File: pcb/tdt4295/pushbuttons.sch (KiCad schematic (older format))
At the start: 4 parts

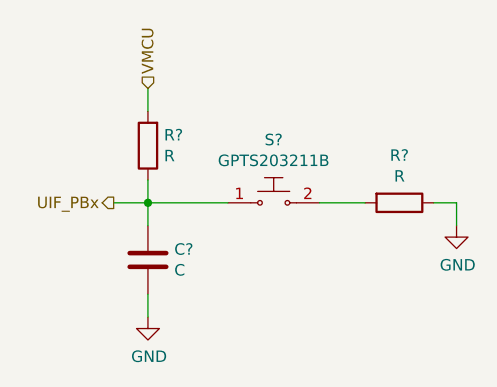
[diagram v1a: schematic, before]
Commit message: add indicator LEDs to power supply
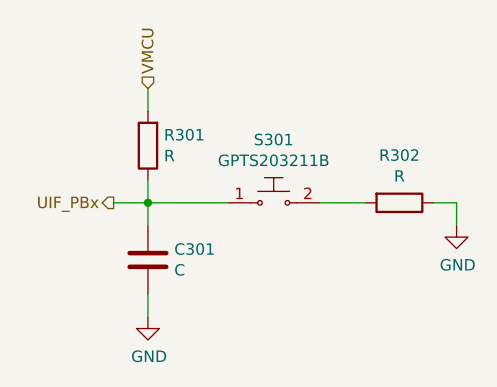
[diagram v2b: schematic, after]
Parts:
- gave numbers to parts that had none: 4
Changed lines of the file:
@@
 $EndDescr
 $Comp
-L Device:R R?
+L Device:R R302
 U 1 1 6137CF49
 P 6650 3150
-F 0 "R?" V 6443 3150 50  0000 C CNN
+F 0 "R302" V 6443 3150 50  0000 C CNN
 F 1 "R" V 6534 3150 50  0000 C CNN
 F 2 "" V 6580 3150 50  0001 C CNN
@@
 $EndComp
 $Comp
-L power:GND #PWR?
+L power:GND #PWR0302
 U 1 1 6137E2C6
 P 6900 3250
-F 0 "#PWR?" H 6900 3000 50  0001 C CNN
+F 0 "#PWR0302" H 6900 3000 50  0001 C CNN
 F 1 "GND" H 6905 3077 50  0000 C CNN
 F 2 "" H 6900 3250 50  0001 C CNN
@@
 $EndComp
 $Comp
-L dk_Pushbutton-Switches:GPTS203211B S?
+L dk_Pushbutton-Switches:GPTS203211B S301
 U 1 1 61381706
 P 6100 3150
-F 0 "S?" H 6100 3425 50  0000 C CNN
+F 0 "S301" H 6100 3425 50  0000 C CNN
 F 1 "GPTS203211B" H 6100 3334 50  0000 C CNN
 F 2 "digikey-footprints:PushButton_12x12mm_THT_GPTS203211B" H 6300 3350 50  0001 L CNN
@@
 $EndComp
 $Comp
-L Device:C C?
+L Device:C C301
 U 1 1 61382E91
 P 5550 3400
-F 0 "C?" H 5665 3446 50  0000 L CNN
+F 0 "C301" H 5665 3446 50  0000 L CNN
 F 1 "C" H 5665 3355 50  0000 L CNN
 F 2 "" H 5588 3250 50  0001 C CNN
@@
 $EndComp
 $Comp
-L Device:R R?
+L Device:R R301
 U 1 1 613838C9
 P 5550 2900
-F 0 "R?" H 5480 2854 50  0000 R CNN
+F 0 "R301" H 5480 2854 50  0000 R CNN
 F 1 "R" H 5480 2945 50  0000 R CNN
 F 2 "" V 5480 2900 50  0001 C CNN
@@
 	5550 3150 5550 3250
 $Comp
-L power:GND #PWR?
+L power:GND #PWR0301
 U 1 1 61384C0F
 P 5550 3650
-F 0 "#PWR?" H 5550 3400 50  0001 C CNN
+F 0 "#PWR0301" H 5550 3400 50  0001 C CNN
 F 1 "GND" H 5555 3477 50  0000 C CNN
 F 2 "" H 5550 3650 50  0001 C CNN
